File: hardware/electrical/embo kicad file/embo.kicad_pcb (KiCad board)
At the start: 2 copper layers, 9 parts, among them U1 TMC2209-LA, U2 ESP32-S3-WROOM-1, U3 AMS1117-3.3, U4 TMC2209-LA, U5 LM2596S-5, U8 AD9833xRM

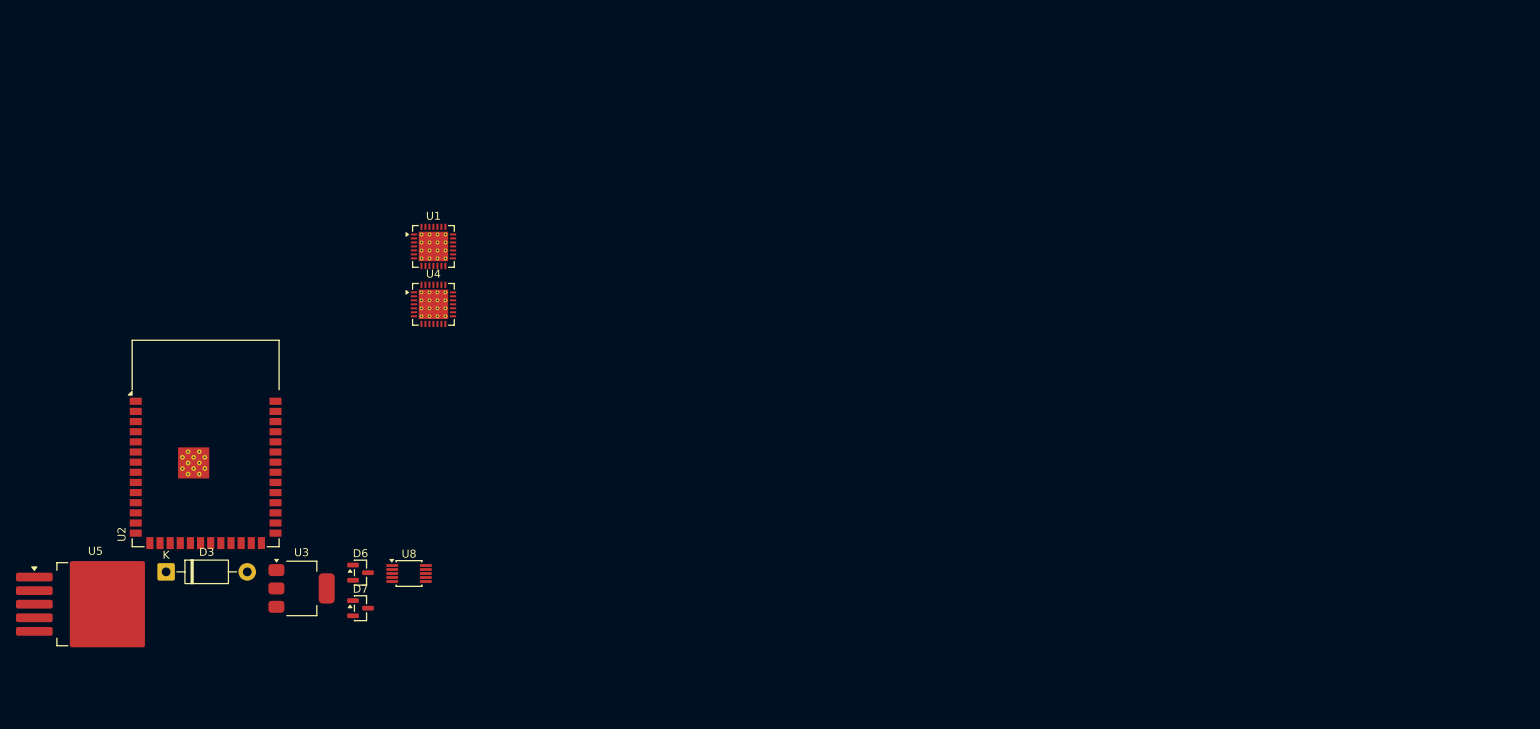
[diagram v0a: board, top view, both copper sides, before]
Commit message: PCB Placement Update
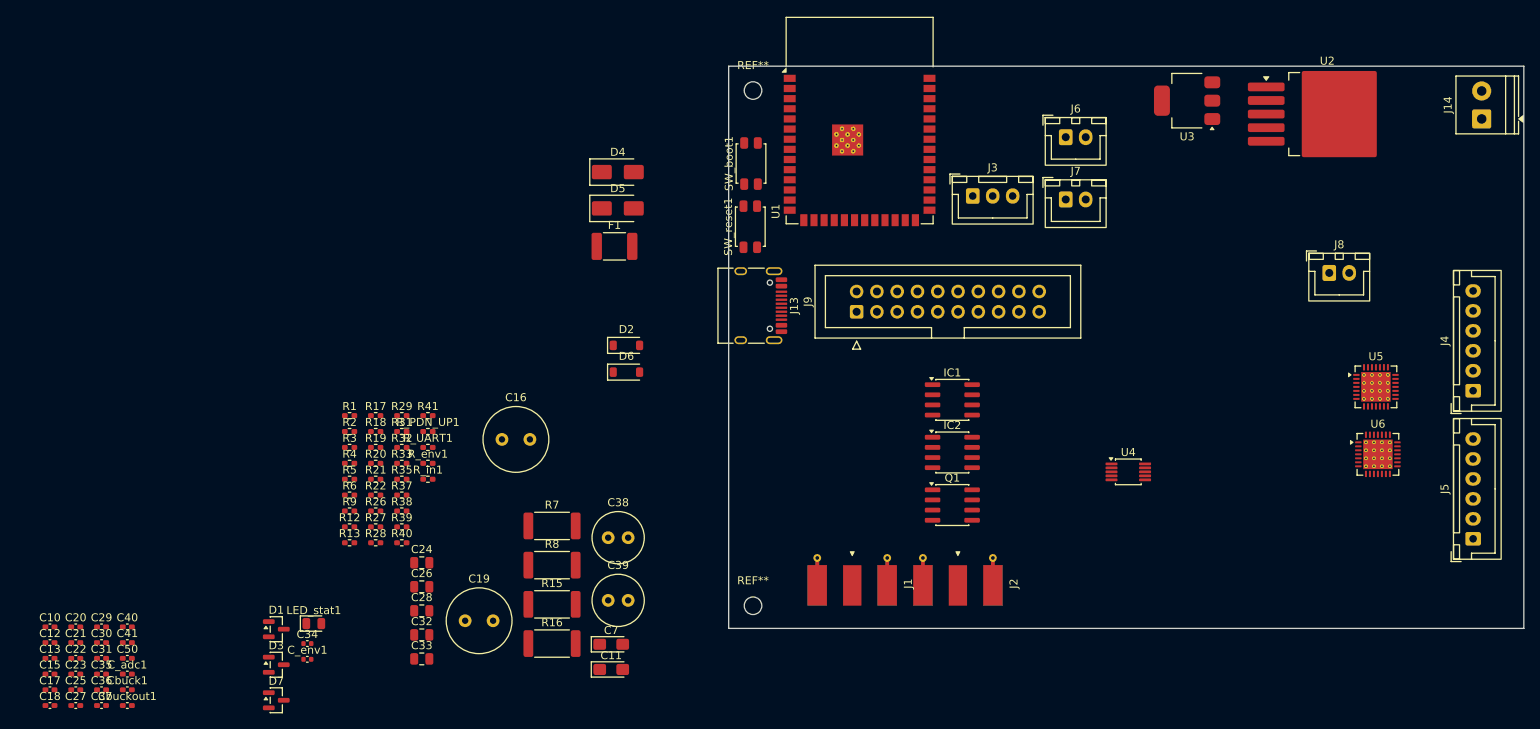
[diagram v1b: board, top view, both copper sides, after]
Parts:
- removed U8: AD9833xRM, Package_SO:MSOP-10_3x3mm_P0.5mm
- added C10: 1µF X7R, Capacitor_SMD:C_0402_1005Metric_Pad0.74x0.62mm_HandSolder, F.Cu at (36.8, 139.9)
- added C11: 10µF 10V tantalum Case A, Capacitor_Tantalum_SMD:CP_EIA-3216-18_Kemet-A_HandSolder, F.Cu at (107.1, 145.2)
- added C12: 100nF X7R, Capacitor_SMD:C_0402_1005Metric_Pad0.74x0.62mm_HandSolder, F.Cu at (36.8, 141.9)
- added C13: 100nF X7R, Capacitor_SMD:C_0402_1005Metric_Pad0.74x0.62mm_HandSolder, F.Cu at (36.8, 143.9)
- added C15: 100nF X7R, Capacitor_SMD:C_0402_1005Metric_Pad0.74x0.62mm_HandSolder, F.Cu at (36.8, 145.8)
- added C16: 100µF 50V electrolytic radial, Capacitor_THT:C_Radial_D8.0mm_H11.5mm_P3.50mm, F.Cu at (93.4, 116.4)
- added C17: 100nF X7R, Capacitor_SMD:C_0402_1005Metric_Pad0.74x0.62mm_HandSolder, F.Cu at (36.8, 147.8)
- added C18: 100nF X7R, Capacitor_SMD:C_0402_1005Metric_Pad0.74x0.62mm_HandSolder, F.Cu at (36.8, 149.8)
- added C19: 220µF 10V low-ESR electrolytic radial, Capacitor_THT:C_Radial_D8.0mm_H11.5mm_P3.50mm, F.Cu at (88.8, 139.1)
- added C20: 100nF X7R, Capacitor_SMD:C_0402_1005Metric_Pad0.74x0.62mm_HandSolder, F.Cu at (40.0, 139.9)
- added C21: 100nF X7R, Capacitor_SMD:C_0402_1005Metric_Pad0.74x0.62mm_HandSolder, F.Cu at (40.0, 141.9)
- added C22: 100nF X7R, Capacitor_SMD:C_0402_1005Metric_Pad0.74x0.62mm_HandSolder, F.Cu at (40.0, 143.9)
- added C23: 100nF X7R, Capacitor_SMD:C_0402_1005Metric_Pad0.74x0.62mm_HandSolder, F.Cu at (40.0, 145.8)
- added C24: 10µF X5R 0805, Capacitor_SMD:C_0805_2012Metric, F.Cu at (83.3, 131.9)
- added C25: 100nF X7R, Capacitor_SMD:C_0402_1005Metric_Pad0.74x0.62mm_HandSolder, F.Cu at (40.0, 147.8)
- added C26: 10µF X5R 0805, Capacitor_SMD:C_0805_2012Metric, F.Cu at (83.3, 134.9)
- added C27: 100nF X7R, Capacitor_SMD:C_0402_1005Metric_Pad0.74x0.62mm_HandSolder, F.Cu at (40.0, 149.8)
- added C28: 10µF X5R 0805, Capacitor_SMD:C_0805_2012Metric, F.Cu at (83.3, 137.9)
- added C29: 100nF X7R, Capacitor_SMD:C_0402_1005Metric_Pad0.74x0.62mm_HandSolder, F.Cu at (43.2, 139.9)
- added C30: 100nF X7R, Capacitor_SMD:C_0402_1005Metric_Pad0.74x0.62mm_HandSolder, F.Cu at (43.2, 141.9)
- added C31: 100nF X7R, Capacitor_SMD:C_0402_1005Metric_Pad0.74x0.62mm_HandSolder, F.Cu at (43.2, 143.9)
- added C32: 10µF X5R 0805, Capacitor_SMD:C_0805_2012Metric, F.Cu at (83.3, 140.9)
- added C33: 10µF X5R 0805, Capacitor_SMD:C_0805_2012Metric, F.Cu at (83.3, 143.9)
- added C34: 10nF X7R, Capacitor_SMD:C_0402_1005Metric, F.Cu at (69.0, 142.0)
- added C35: 100nF X7R, Capacitor_SMD:C_0402_1005Metric_Pad0.74x0.62mm_HandSolder, F.Cu at (43.2, 145.8)
- added C36: 100nF X7R, Capacitor_SMD:C_0402_1005Metric_Pad0.74x0.62mm_HandSolder, F.Cu at (43.2, 147.8)
- added C37: 100nF X7R, Capacitor_SMD:C_0402_1005Metric_Pad0.74x0.62mm_HandSolder, F.Cu at (43.2, 149.8)
- added C38: 100µF 35V electrolytic radial, Capacitor_THT:C_Radial_D6.3mm_H11.0mm_P2.50mm, F.Cu at (106.7, 128.7)
- added C39: 100µF 35V electrolytic radial, Capacitor_THT:C_Radial_D6.3mm_H11.0mm_P2.50mm, F.Cu at (106.7, 136.6)
- added C40: 100nF X7R, Capacitor_SMD:C_0402_1005Metric_Pad0.74x0.62mm_HandSolder, F.Cu at (46.5, 139.9)
- added C41: 100nF X7R, Capacitor_SMD:C_0402_1005Metric_Pad0.74x0.62mm_HandSolder, F.Cu at (46.5, 141.9)
- added C50: 1nF X7R, Capacitor_SMD:C_0402_1005Metric_Pad0.74x0.62mm_HandSolder, F.Cu at (46.5, 143.9)
- added C7: 10µF 10V tantalum Case A, Capacitor_Tantalum_SMD:CP_EIA-3216-18_Kemet-A_HandSolder, F.Cu at (107.1, 142.1)
- added C_adc1: 100nF X7R, Capacitor_SMD:C_0402_1005Metric_Pad0.74x0.62mm_HandSolder, F.Cu at (46.5, 145.8)
- added C_env1: 10nF X7R, Capacitor_SMD:C_0402_1005Metric, F.Cu at (69.0, 144.0)
- added Cbuck1: 100nF X7R, Capacitor_SMD:C_0402_1005Metric_Pad0.74x0.62mm_HandSolder, F.Cu at (46.5, 147.8)
- added Cbuckout1: 100nF X7R, Capacitor_SMD:C_0402_1005Metric_Pad0.74x0.62mm_HandSolder, F.Cu at (46.5, 149.8)
- added D1: BAV99, Package_TO_SOT_SMD:SOT-23, F.Cu at (65.1, 140.2)
- added D2: BAT54, Diode_SMD:D_SOD-123, F.Cu at (109.0, 104.7)
- added D4: SS34A, Diode_SMD:D_SMA, F.Cu at (107.9, 83.0)
- added D5: SMBJ28A, Diode_SMD:D_SMA, F.Cu at (107.9, 87.5)
- added F1: 1A polyfuse (1812), Fuse:Fuse_1812_4532Metric_Pad1.30x3.40mm_HandSolder, F.Cu at (107.5, 92.3)
- added IC1: OPA2354, Package_SO:SOIC-8_3.9x4.9mm_P1.27mm, F.Cu at (149.8, 111.5)
- added IC2: OPA2354, Package_SO:SOIC-8_3.9x4.9mm_P1.27mm, F.Cu at (149.8, 118.1)
- added J1: Conn_Coaxial, Connector_Coaxial:SMA_Molex_73251-1153_EdgeMount_Horizontal, F.Cu at (137.3, 133.0)
- added J13: USB_C_Receptacle_USB2.0_16P, Connector_USB:USB_C_Receptacle_HRO_TYPE-C-31-M-12, F.Cu at (124.3, 99.7)
- added J14: 24 V PSU input, TerminalBlock_Phoenix:TerminalBlock_Phoenix_PT-1,5-2-3.5-H_1x02_P3.50mm_Horizontal, F.Cu at (216.1, 76.3)
- added J2: Conn_Coaxial, Connector_Coaxial:SMA_Molex_73251-1153_EdgeMount_Horizontal, F.Cu at (150.5, 133.0)
- added J3: UART to RPi, Connector_JST:JST_XH_B3B-XH-A_1x03_P2.50mm_Vertical, F.Cu at (152.3, 86.0)
- added J4: JSTXH 6pin Socket 1, Connector_JST:JST_XH_B6B-XH-A_1x06_P2.50mm_Vertical, F.Cu at (215.0, 110.3)
- added J5: JSTXH 6pin Socket 2, Connector_JST:JST_XH_B6B-XH-A_1x06_P2.50mm_Vertical, F.Cu at (215.0, 128.9)
- added J6: motor 1, Connector_JST:JST_XH_B2B-XH-A_1x02_P2.50mm_Vertical, F.Cu at (164.0, 78.6)
- added J7: motor 2, Connector_JST:JST_XH_B2B-XH-A_1x02_P2.50mm_Vertical, F.Cu at (164.0, 86.4)
- added J8: LED Panel, Connector_JST:JST_XH_B2B-XH-A_1x02_P2.50mm_Vertical, F.Cu at (197.0, 95.6)
- added J9: Conn_02x10_Odd_Even, Connector_IDC:IDC-Header_2x10_P2.54mm_Vertical, F.Cu at (137.8, 100.5)
- added LED_stat1: green LED, LED_SMD:LED_0805_2012Metric, F.Cu at (69.8, 139.5)
- added Q1: AO4407A, Package_SO:SOIC-8_3.9x4.9mm_P1.27mm, F.Cu at (149.8, 124.7)
- added R1: 10kΩ, Resistor_SMD:R_0402_1005Metric_Pad0.72x0.64mm_HandSolder, F.Cu at (74.3, 113.5)
- added R12: 10kΩ, Resistor_SMD:R_0402_1005Metric_Pad0.72x0.64mm_HandSolder, F.Cu at (74.3, 127.4)
- added R13: 10kΩ, Resistor_SMD:R_0402_1005Metric_Pad0.72x0.64mm_HandSolder, F.Cu at (74.3, 129.4)
- added R15: 0.11Ω, Resistor_SMD:R_2512_6332Metric, F.Cu at (99.7, 137.1)
- added R16: 0.11Ω, Resistor_SMD:R_2512_6332Metric, F.Cu at (99.7, 142.0)
- added R17: 5.1kΩ, Resistor_SMD:R_0402_1005Metric_Pad0.72x0.64mm_HandSolder, F.Cu at (77.6, 113.5)
- added R18: 5.1kΩ, Resistor_SMD:R_0402_1005Metric_Pad0.72x0.64mm_HandSolder, F.Cu at (77.6, 115.5)
- added R19: 4.7kΩ, Resistor_SMD:R_0402_1005Metric_Pad0.72x0.64mm_HandSolder, F.Cu at (77.6, 117.4)
- added R2: 10kΩ, Resistor_SMD:R_0402_1005Metric_Pad0.72x0.64mm_HandSolder, F.Cu at (74.3, 115.5)
- added R20: 10kΩ, Resistor_SMD:R_0402_1005Metric_Pad0.72x0.64mm_HandSolder, F.Cu at (77.6, 119.4)
- added R21: 10kΩ, Resistor_SMD:R_0402_1005Metric_Pad0.72x0.64mm_HandSolder, F.Cu at (77.6, 121.4)
- added R22: 10kΩ, Resistor_SMD:R_0402_1005Metric_Pad0.72x0.64mm_HandSolder, F.Cu at (77.6, 123.4)
- added R26: 100Ω, Resistor_SMD:R_0402_1005Metric_Pad0.72x0.64mm_HandSolder, F.Cu at (77.6, 125.4)
- added R27: 910Ω, Resistor_SMD:R_0402_1005Metric_Pad0.72x0.64mm_HandSolder, F.Cu at (77.6, 127.4)
- added R28: 10kΩ, Resistor_SMD:R_0402_1005Metric_Pad0.72x0.64mm_HandSolder, F.Cu at (77.6, 129.4)
- added R29: 10kΩ, Resistor_SMD:R_0402_1005Metric_Pad0.72x0.64mm_HandSolder, F.Cu at (80.8, 113.5)
- added R3: 10kΩ, Resistor_SMD:R_0402_1005Metric_Pad0.72x0.64mm_HandSolder, F.Cu at (74.3, 117.4)
- added R31: 100Ω, Resistor_SMD:R_0402_1005Metric_Pad0.72x0.64mm_HandSolder, F.Cu at (80.8, 115.5)
- added R32: 47Ω, Resistor_SMD:R_0402_1005Metric_Pad0.72x0.64mm_HandSolder, F.Cu at (80.8, 117.4)
- added R33: 390Ω, Resistor_SMD:R_0402_1005Metric_Pad0.72x0.64mm_HandSolder, F.Cu at (80.8, 119.4)
- added R35: 910Ω, Resistor_SMD:R_0402_1005Metric_Pad0.72x0.64mm_HandSolder, F.Cu at (80.8, 121.4)
- added R37: 100Ω, Resistor_SMD:R_0402_1005Metric_Pad0.72x0.64mm_HandSolder, F.Cu at (80.8, 123.4)
- added R38: 10kΩ, Resistor_SMD:R_0402_1005Metric_Pad0.72x0.64mm_HandSolder, F.Cu at (80.8, 125.4)
- added R39: 10kΩ, Resistor_SMD:R_0402_1005Metric_Pad0.72x0.64mm_HandSolder, F.Cu at (80.8, 127.4)
- added R4: 10kΩ, Resistor_SMD:R_0402_1005Metric_Pad0.72x0.64mm_HandSolder, F.Cu at (74.3, 119.4)
- added R40: 10kΩ 0402, Resistor_SMD:R_0402_1005Metric_Pad0.72x0.64mm_HandSolder, F.Cu at (80.8, 129.4)
- added R41: 10kΩ 0402, Resistor_SMD:R_0402_1005Metric_Pad0.72x0.64mm_HandSolder, F.Cu at (84.1, 113.5)
- added R5: 10kΩ 0402, Resistor_SMD:R_0402_1005Metric_Pad0.72x0.64mm_HandSolder, F.Cu at (74.3, 121.4)
- added R6: 330Ω, Resistor_SMD:R_0402_1005Metric_Pad0.72x0.64mm_HandSolder, F.Cu at (74.3, 123.4)
- added R7: 0.11Ω, Resistor_SMD:R_2512_6332Metric, F.Cu at (99.7, 127.3)
- added R8: 0.11Ω, Resistor_SMD:R_2512_6332Metric, F.Cu at (99.7, 132.2)
- added R9: 10kΩ, Resistor_SMD:R_0402_1005Metric_Pad0.72x0.64mm_HandSolder, F.Cu at (74.3, 125.4)
- added REF**: MountingHole_2.2mm_M2, MountingHole:MountingHole_2.2mm_M2, F.Cu at (124.8, 72.8)
- added REF**: MountingHole_2.2mm_M2, MountingHole:MountingHole_2.2mm_M2, F.Cu at (124.8, 137.3)
- added R_PDN_UP1: 10kΩ 0402, Resistor_SMD:R_0402_1005Metric_Pad0.72x0.64mm_HandSolder, F.Cu at (84.1, 115.5)
- added R_UART1: 1kΩ 0402, Resistor_SMD:R_0402_1005Metric_Pad0.72x0.64mm_HandSolder, F.Cu at (84.1, 117.4)
- added R_env1: 10kΩ 0402, Resistor_SMD:R_0402_1005Metric_Pad0.72x0.64mm_HandSolder, F.Cu at (84.1, 119.4)
- added R_in1: 100Ω 0402, Resistor_SMD:R_0402_1005Metric_Pad0.72x0.64mm_HandSolder, F.Cu at (84.1, 121.4)
- added SW_boot1: 6×6mm tactile, Button_Switch_SMD:SW_SPST_EVQP2_MiddlePushTravel_H2.5mm, F.Cu at (124.6, 81.9)
- added SW_reset1: 6×6mm tactile, Button_Switch_SMD:SW_SPST_EVQP2_MiddlePushTravel_H2.5mm, F.Cu at (124.5, 89.8)
- added U6: TMC2209-LA, Package_DFN_QFN:VQFN-28-1EP_5x5mm_P0.5mm_EP3.7x3.7mm_ThermalVias, F.Cu at (203.1, 118.3)
- D3: value 1N5819 -> BAV99; footprint Diode_THT:D_DO-41_SOD81_P10.16mm_Horizontal -> Package_TO_SOT_SMD:SOT-23
- D6: value BAV99 -> 1N5819; footprint Package_TO_SOT_SMD:SOT-23 -> Diode_SMD:D_SOD-123
- D7: value BAV99 -> BZX84C15
- U1: value TMC2209-LA -> ESP32-S3-WROOM-1; footprint Package_DFN_QFN:VQFN-28-1EP_5x5mm_P0.5mm_EP3.7x3.7mm_ThermalVias -> RF_Module:ESP32-S3-WROOM-1
- U2: value ESP32-S3-WROOM-1 -> LM2596S-5; footprint RF_Module:ESP32-S3-WROOM-1 -> Package_TO_SOT_SMD:TO-263-5_TabPin3
- U4: value TMC2209-LA -> AD9833xRM; footprint Package_DFN_QFN:VQFN-28-1EP_5x5mm_P0.5mm_EP3.7x3.7mm_ThermalVias -> Package_SO:MSOP-10_3x3mm_P0.5mm
- U5: value LM2596S-5 -> TMC2209-LA; footprint Package_TO_SOT_SMD:TO-263-5_TabPin3 -> Package_DFN_QFN:VQFN-28-1EP_5x5mm_P0.5mm_EP3.7x3.7mm_ThermalVias
- moved U5 162.6 mm to (202.8, 109.9)
- moved U2 146.4 mm to (196.7, 75.7)
- moved U3 126.6 mm to (179.2, 74.0), turned to 180 degrees
- moved U4 89.5 mm to (171.8, 120.5)
- moved U1 55.7 mm to (138.2, 76.5)
- moved D6 41.7 mm to (109.0, 108.0)
- moved D3 18.0 mm to (65.1, 144.7)
- moved D7 15.6 mm to (65.1, 149.1)
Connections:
- D3 pad 1: +5V -> GND
- D3 pad 2: Net-(D3-A) -> +3V3
- D6 pad 1: GND -> +5V
- D6 pad 2: +3V3 -> Net-(D6-A)
- D7 pad 1: GND -> Net-(D7-K)
- D7 pad 2: +3V3 -> Net-(D7-A)
- D7 pad 3: /RX_AMP_IN -> (no net)
- U1 pad 1: /M1_B2 -> GND
- U1 pad 10: GND -> /EC11_B (DT)
- U1 pad 11: Net-(U1-DIAG) -> /EC11_SW
- U1 pad 12: Net-(U1-INDEX) -> /M2_STEP
- U1 pad 13: unconnected-(U1-CLK-Pad13) -> /USB_D-
- U1 pad 14: /TMC_UART -> /USB_D+
- U1 pad 15: +3V3 -> unconnected-(U1-IO3-Pad15)
- U1 pad 16: /M1_STEP -> unconnected-(U1-IO46-Pad16)
- U1 pad 17: unconnected-(U1-VREF-Pad17) -> /M2_DIR
- U1 pad 18: GND -> /M2_EN
- U1 pad 19: /M1_DIR -> /BTN1
- U1 pad 2: /M1_EN -> +3V3
- U1 pad 20: unconnected-(U1-STDBY-Pad20) -> /BTN2
- U1 pad 21: /M1_A2 -> /BUZ_PWM
- U1 pad 22: +24V -> /LIMIT_M1
- U1 pad 23: Net-(U1-BRA) -> /TOUCH_IRQ
- U1 pad 24: /M1_A1 -> /UART_TX
- U1 pad 25: unconnected-(U1-NC-Pad25) -> /UART_RX
- U1 pad 26: /M1_B1 -> unconnected-(U1-IO45-Pad26)
- U1 pad 28: +24V -> /SPI_MOSI
- U1 pad 29: GND -> /SPI_CLK
- U1 pad 3: GND -> Net-(U1-EN)
- U1 pad 4: unconnected-(U1-CPO-Pad4) -> /TMC_UART
- U1 pad 5: unconnected-(U1-CPI-Pad5) -> /M1_STEP
- U1 pad 6: Net-(U1-VCP) -> /M1_DIR
- U1 pad 7: Net-(U1-SPREAD) -> /M1_EN
- U1 pad 8: unconnected-(U1-5VOUT-Pad8) -> /LIMIT_M2
- U1 pad 9: GND -> /EC11_A (CLK)
- U2 pad 1: GND -> +24V
- U2 pad 2: +3V3 -> Net-(D4-K)
- U2 pad 3: unconnected-(U2-EN-Pad3) -> GND
- U2 pad 4: /TMC_UART -> +5V
- U2 pad 5: /M1_STEP -> GND
- U4 pad 1: /M2_B2 -> Net-(U4-COMP)
- U4 pad 10: GND -> /TX_AMP_IN
- U4 pad 2: /M2_EN -> +3V3
- U4 pad 3: GND -> Net-(U4-CAP/2.5V)
- U4 pad 4: unconnected-(U4-CPO-Pad4) -> GND
- U4 pad 6: Net-(U4-VCP) -> /SPI_MOSI
- U4 pad 7: Net-(U4-SPREAD) -> /SPI_CLK
- U4 pad 8: unconnected-(U4-5VOUT-Pad8) -> /AD9833_SC
- U4 pad 9: Net-(U4-MS1/AD0) -> GND
- U5 pad 1: +24V -> /M1_B2
- U5 pad 2: Net-(D4-A) -> /M1_EN
- U5 pad 4: +5V -> unconnected-(U5-CPO-Pad4)
- U5 pad 5: GND -> unconnected-(U5-CPI-Pad5)
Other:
- board outline added: 99.6 x 70.4 mm

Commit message: PCB layout update
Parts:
- added L1: 100µH, Inductor_SMD:L_Bourns_SRR1260, F.Cu at (182.3, 85.9)
- moved D7 156.2 mm to (206.3, 82.3)
- moved C16 119.9 mm to (205.0, 72.7), turned to -90 degrees
- moved C19 109.5 mm to (176.0, 73.0), turned to -90 degrees
- moved F1 105.8 mm to (212.9, 82.9)
- moved D5 105.8 mm to (213.3, 78.1)
- moved C38 102.4 mm to (205.2, 101.0), turned to -90 degrees
- moved C_env1 93.3 mm to (156.9, 112.5)
- moved LED_stat1 93.3 mm to (157.7, 108.1)
- moved C34 93.3 mm to (156.9, 110.6)
- moved C39 89.6 mm to (189.0, 101.2), turned to -90 degrees
- moved D3 88.5 mm to (136.9, 93.0)
- moved D1 83.9 mm to (136.9, 96.8)
- moved Q1 81.5 mm to (213.4, 73.7)
- moved D4 77.5 mm to (185.1, 77.2), turned to 180 degrees
- moved C10 61.0 mm to (75.5, 92.8)
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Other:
- board size 99.6 x 70.4 mm -> 96.4 x 46.6 mm
